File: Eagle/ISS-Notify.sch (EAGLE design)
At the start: 27 parts, among them J1 AVRISP, U1 ATMEGA32U4, U2 MCP7940N, U3 TPS63001, X2 32.768 kHz

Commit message: power side of schematic
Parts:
- added D1, D2: DIODE, ISS-Notify:DIODE
- added R6: 2 k, rcl_custom:R-US_0603-C-NOSILK
- added SW1: 9077-1, ISS-Notify:9077-1
- added U4: MCP73811, ISS-Notify:MCP73811
- added X1: CX5Z, ISS-Notify:CX5Z
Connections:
- new net N$12: R6.2, U4.PROG
- new net N$13: D1.A, U4.VBAT
- new net N$14: COINCELL.VBAT, D2.A
- new net N$15: D2.C, U2.VBAT
- new net N$6: C5.1, X1.1
- new net N$9: CF1.1, D1.C, SW1.P, U4.CE, U4.VIN
- net GND: now also COINCELL.GND, R6.1, U4.VSS
- net N$10: now also U1.XTAL1, X1.2
- net VIN: now also SW1.S
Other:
- moved on the sheet: C1, C10, C11, C12, C13, C2, C3, C4, C5, C6, C7, C8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

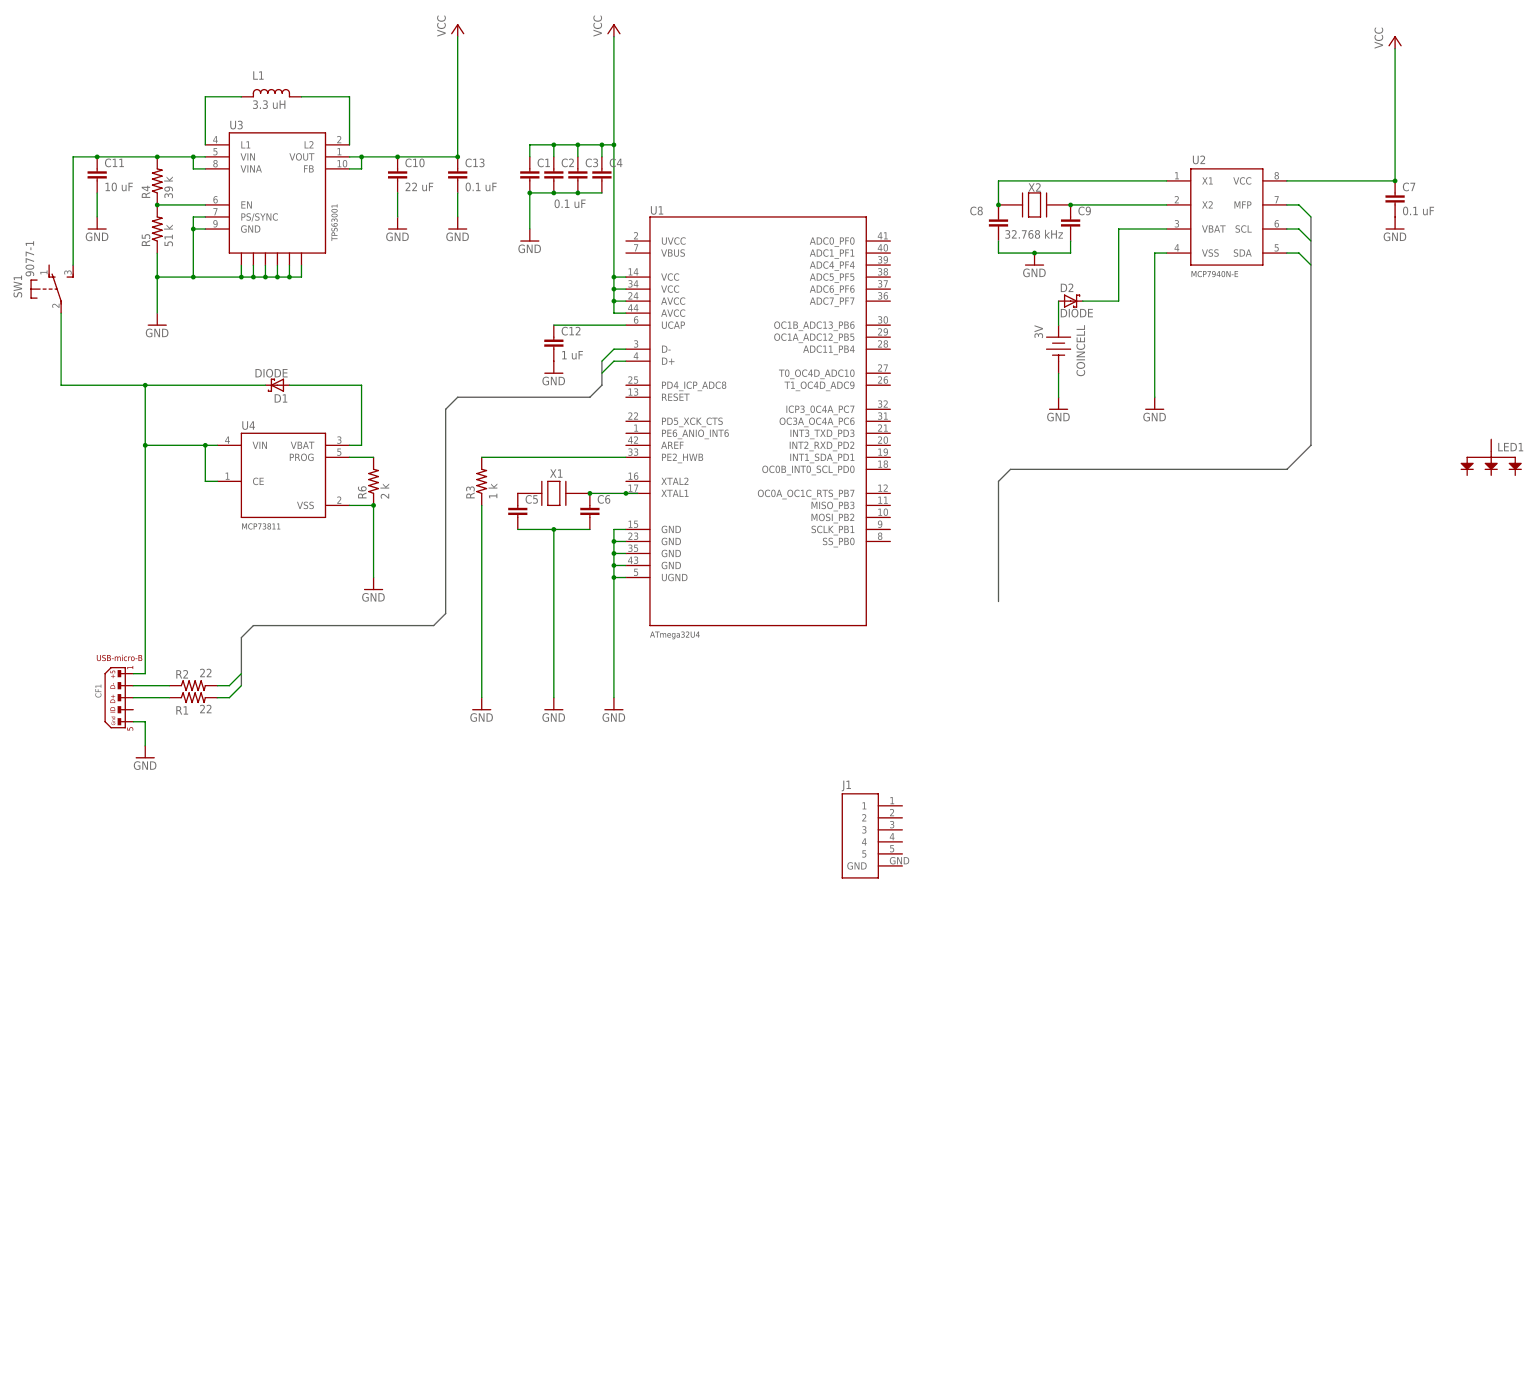
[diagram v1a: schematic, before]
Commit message: LED and drivers in schematic
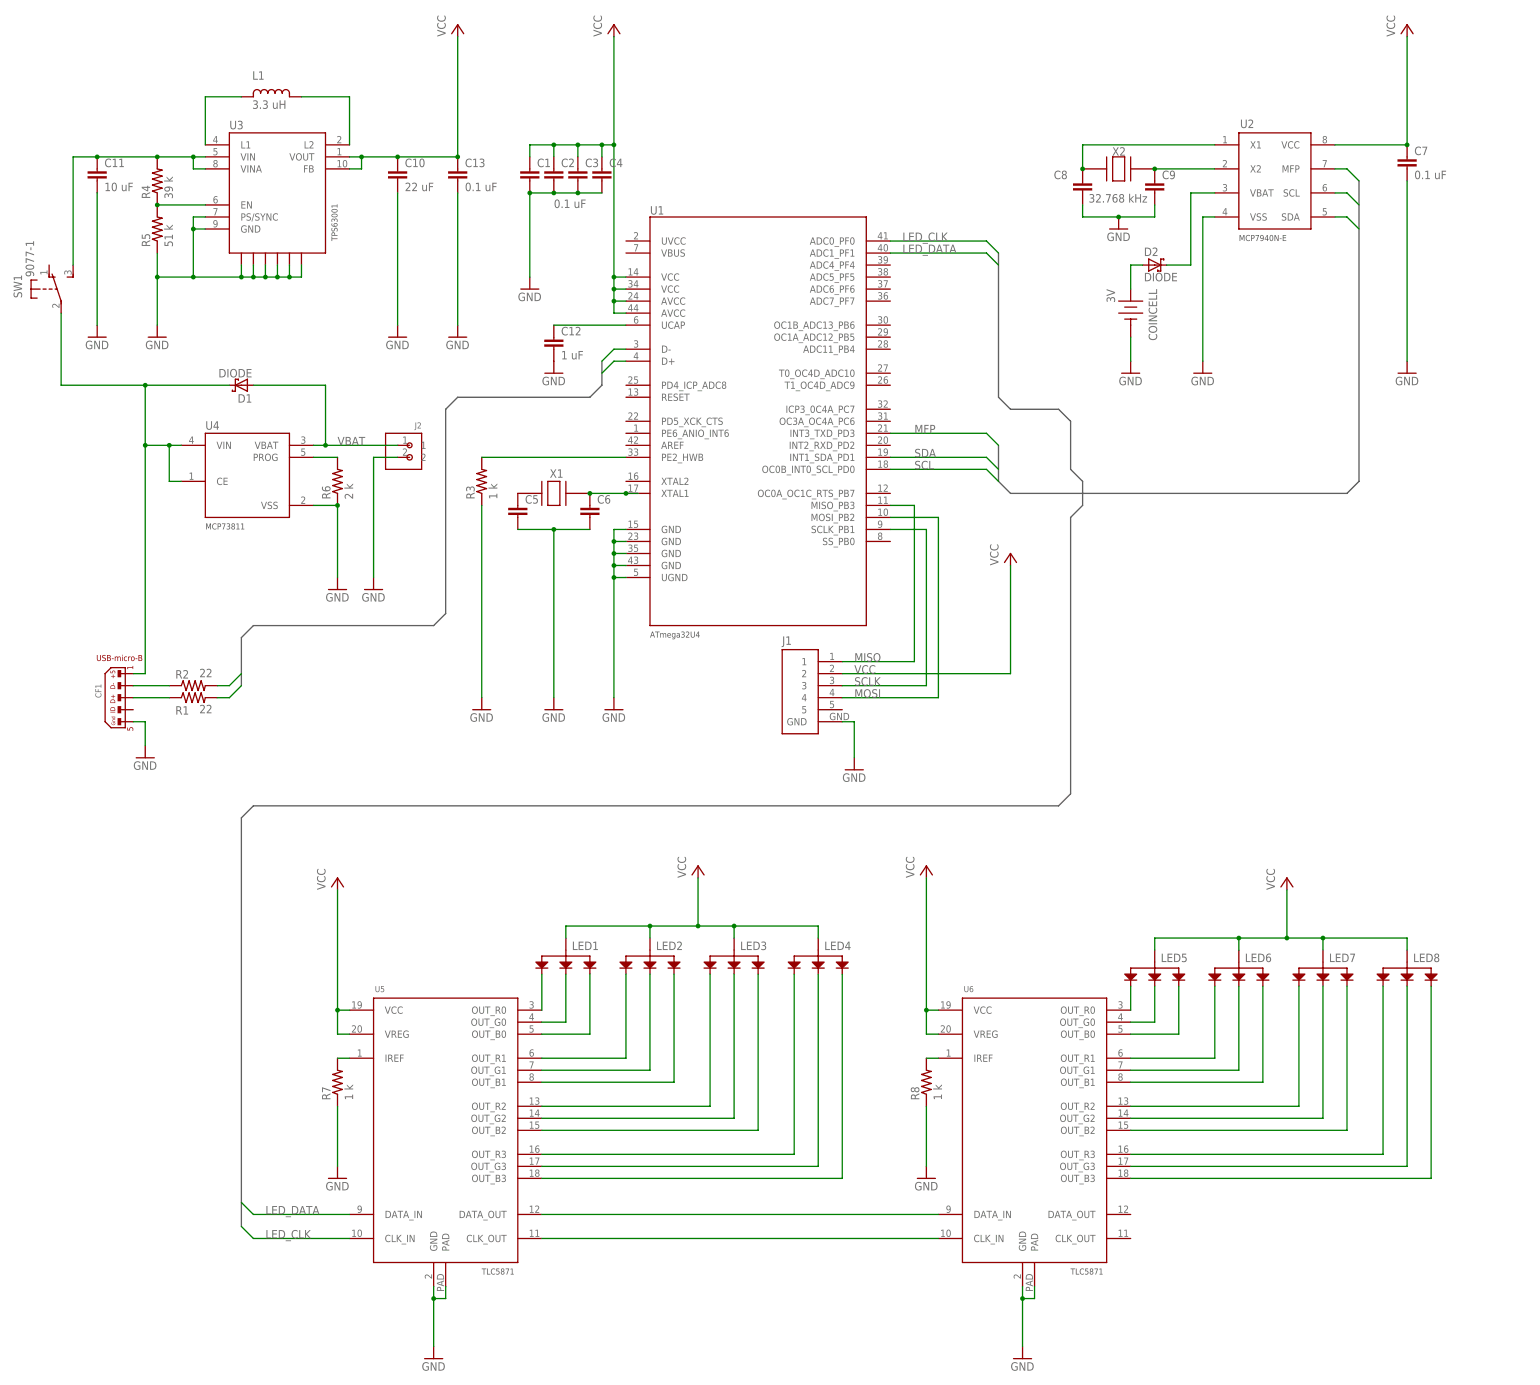
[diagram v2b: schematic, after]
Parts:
- added J2: JST2, ISS-Notify:JST2
- added LED2, LED3, LED4, LED5, LED6, LED7, LED8: RGBLED, ISS-Notify:RGBLED
- added R7, R8: 1 k, rcl_custom:R-US_0603-C-NOSILK
- added U5, U6: TLC5971, ISS-Notify:TLC5971
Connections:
- new net LED_CLK: U1.ADC0_PF0, U5.CLK_IN
- new net LED_DATA: U1.ADC1_PF1, U5.DATA_IN
- new net MISO: J1.1, U1.MISO_PB3
- new net MOSI: J1.4, U1.MOSI_PB2
- new net N$14: U5.DATA_OUT, U6.DATA_IN
- new net N$16: LED2.B, U5.OUT_B1
- new net N$17: R7.2, U5.IREF
- new net N$18: R8.2, U6.IREF
- new net N$19: LED3.R, U5.OUT_R2
- new net N$20: LED3.G, U5.OUT_G2
- new net N$21: LED3.B, U5.OUT_B2
- new net N$22: LED1.R, U5.OUT_R0
- new net N$23: LED1.G, U5.OUT_G0
- new net N$24: LED1.B, U5.OUT_B0
- new net N$25: LED2.R, U5.OUT_R1
- new net N$26: LED2.G, U5.OUT_G1
- new net N$27: LED4.R, U5.OUT_R3
- new net N$28: LED4.G, U5.OUT_G3
- new net N$29: LED4.B, U5.OUT_B3
- new net N$30: LED7.R, U6.OUT_R2
- new net N$31: LED5.R, U6.OUT_R0
- new net N$32: LED5.G, U6.OUT_G0
- new net N$33: LED5.B, U6.OUT_B0
- new net N$34: LED6.R, U6.OUT_R1
- new net N$35: LED6.G, U6.OUT_G1
- new net N$36: LED6.B, U6.OUT_B1
- new net N$37: LED7.G, U6.OUT_G2
- new net N$38: LED7.B, U6.OUT_B2
- new net N$39: LED8.R, U6.OUT_R3
- new net N$40: LED8.G, U6.OUT_G3
- new net N$41: LED8.B, U6.OUT_B3
- new net SCLK: J1.3, U1.SCLK_PB1
- new net VBAT: D1.A, J2.1, U4.VBAT
- net GND: now also J1.GND, J2.2, R7.1, R8.1, U5.GND, U5.PAD, U6.GND, U6.PAD
- net MFP: now also U1.INT3_TXD_PD3
- net N$13: now also U5.CLK_OUT, U6.CLK_IN; no longer D1.A, U4.VBAT
- net SCL: now also U1.OC0B_INT0_SCL_PD0
- net VCC: now also J1.2, LED1.ANODE, LED2.ANODE, LED3.ANODE, LED4.ANODE, LED5.ANODE, LED6.ANODE, LED7.ANODE, LED8.ANODE, U5.VCC, U5.VREG, U6.VCC, U6.VREG
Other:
- moved on the sheet: C7, C8, C9, COINCELL, D1, D2, J1, LED1, R6, U2, U4, X2

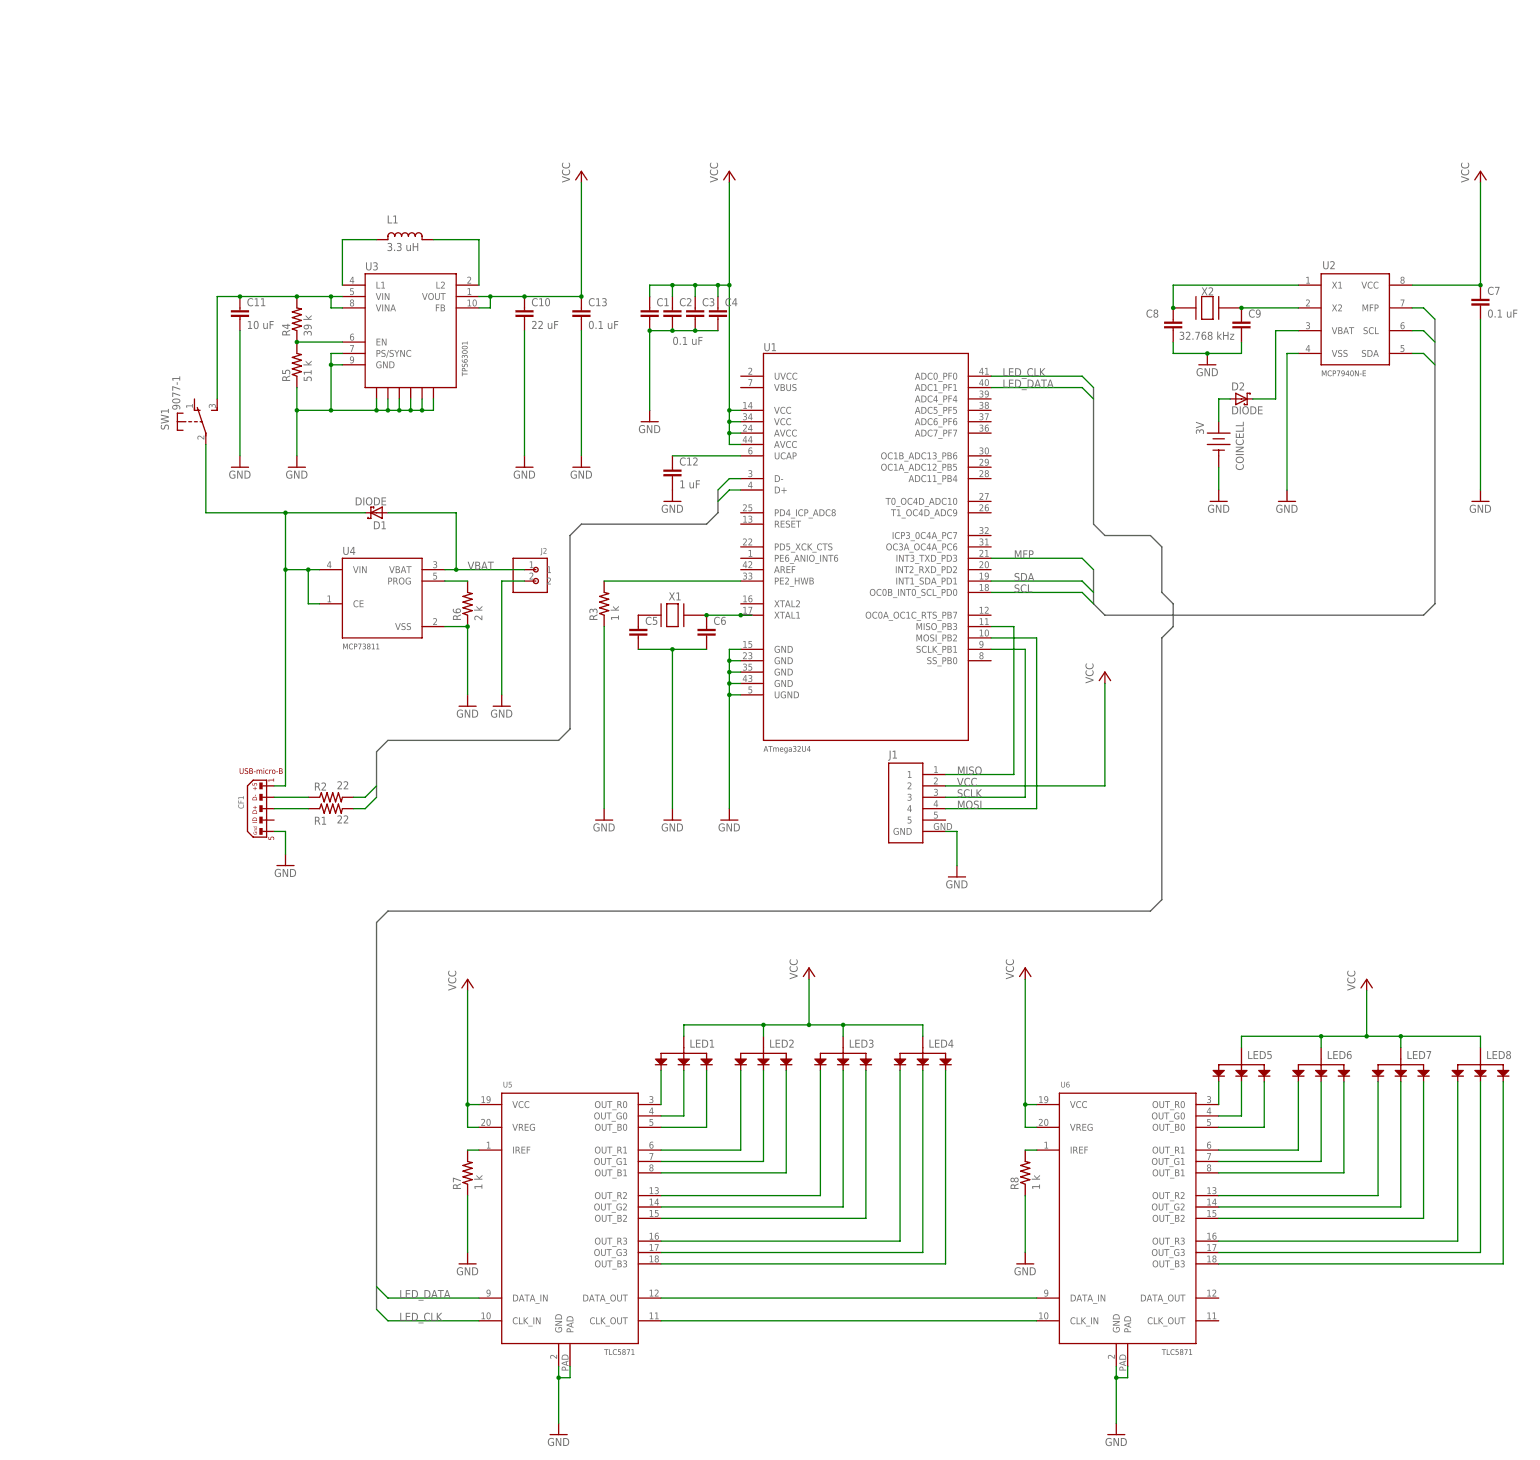
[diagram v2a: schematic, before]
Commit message: LED driver datasheet, Frame and proto header on schematic
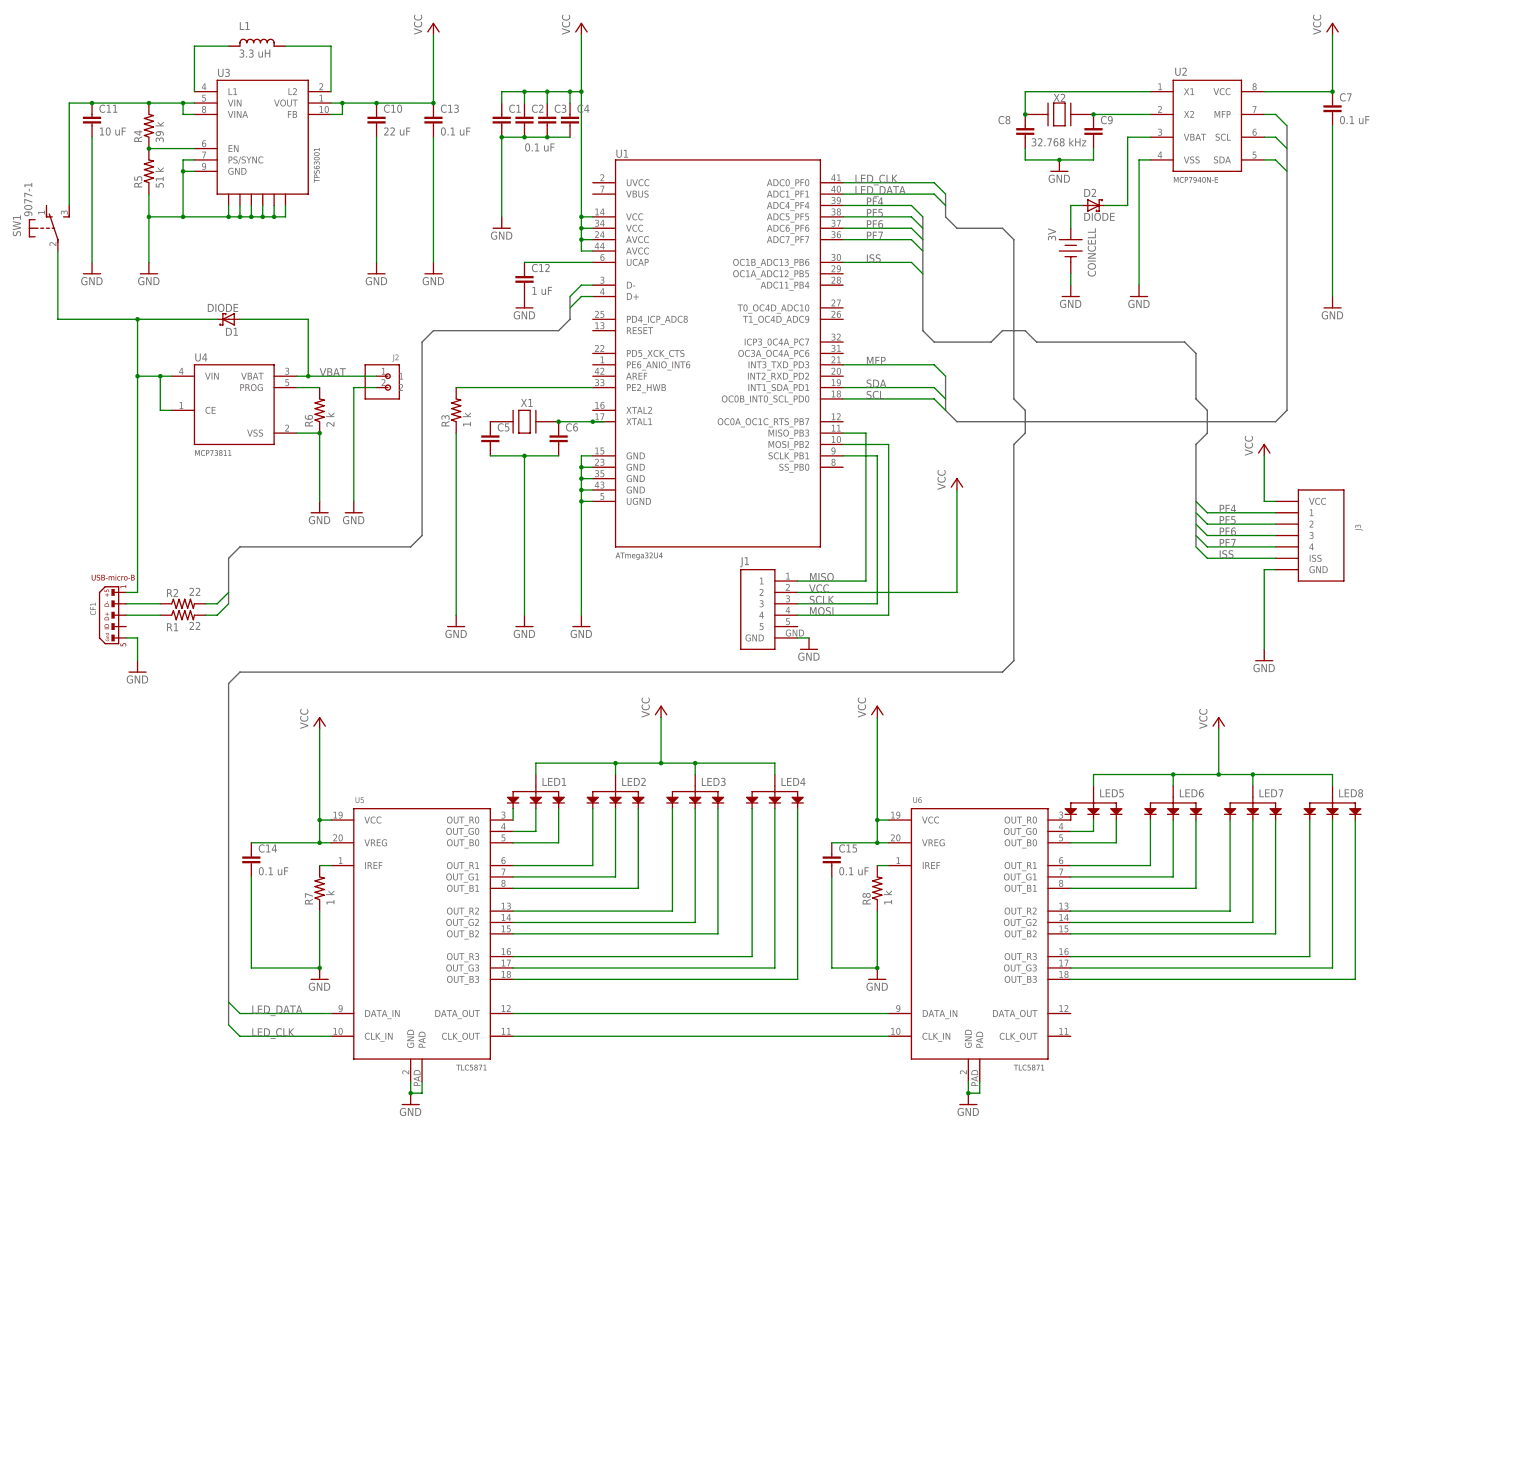
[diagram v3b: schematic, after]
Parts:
- added C14, C15: 0.1 uF, rcl_custom:C-EU0603-C-NOSILK
- added J3: PROTOSPACE2, ISS-Notify:PROTOSPACE2
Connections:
- new net ISS: J3.ISS, U1.OC1B_ADC13_PB6
- new net PF4: J3.1, U1.ADC4_PF4
- new net PF5: J3.2, U1.ADC5_PF5
- new net PF6: J3.3, U1.ADC6_PF6
- new net PF7: J3.4, U1.ADC7_PF7
- net GND: now also C14.2, C15.2, J3.GND
- net SDA: now also U1.INT1_SDA_PD1
- net VCC: now also C14.1, C15.1, J3.VCC
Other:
- moved on the sheet: C1, C10, C11, C12, C13, C2, C3, C4, C5, C6, C7, C8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

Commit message: finish schematic
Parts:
- added C16: 100 pF, rcl_custom:C-EU0603-C-NOSILK
- added SW2: SWITCH, ISS-Notify:SWITCH
- added U$1, U$2, U$3, U$4: _4-BARE_MOUNTING_HOLE/.300, ISS-Notify:_4-BARE_MOUNTING_HOLE/.300
- C8: value (none) -> 10 pF
- C9: value (none) -> 12 pF
- USB: value (none) -> CON_USB-MICRO-6GND
- X1: value CX5Z -> 8 MHz
- renumbered CF1 to USB
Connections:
- net N$9 renamed VUSB
- net PE2_HWB renamed N$42
- removed net UCAP: C12.1, U1.UCAP
- new net RESET: J1.5, SW2.1, U1.RESET
- net GND: now also C16.2, SW2.2
- net N$15: now also C16.1
- net N$6: now also U1.XTAL2
- net VCC: now also C12.1, U1.UCAP
- net VIN: now also U1.VBUS
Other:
- note added: "AVR Microcontroller"
- note added: "Breakout Header"
- note added: "Color LEDs"
- note added: "LiPo Charger"
- note added: "Power"
- note added: "Real Time Clock"
- moved on the sheet: C1, C12, C2, C3, C4, R3
